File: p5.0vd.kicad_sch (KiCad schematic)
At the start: 11 parts, among them U14 LT3045xDD

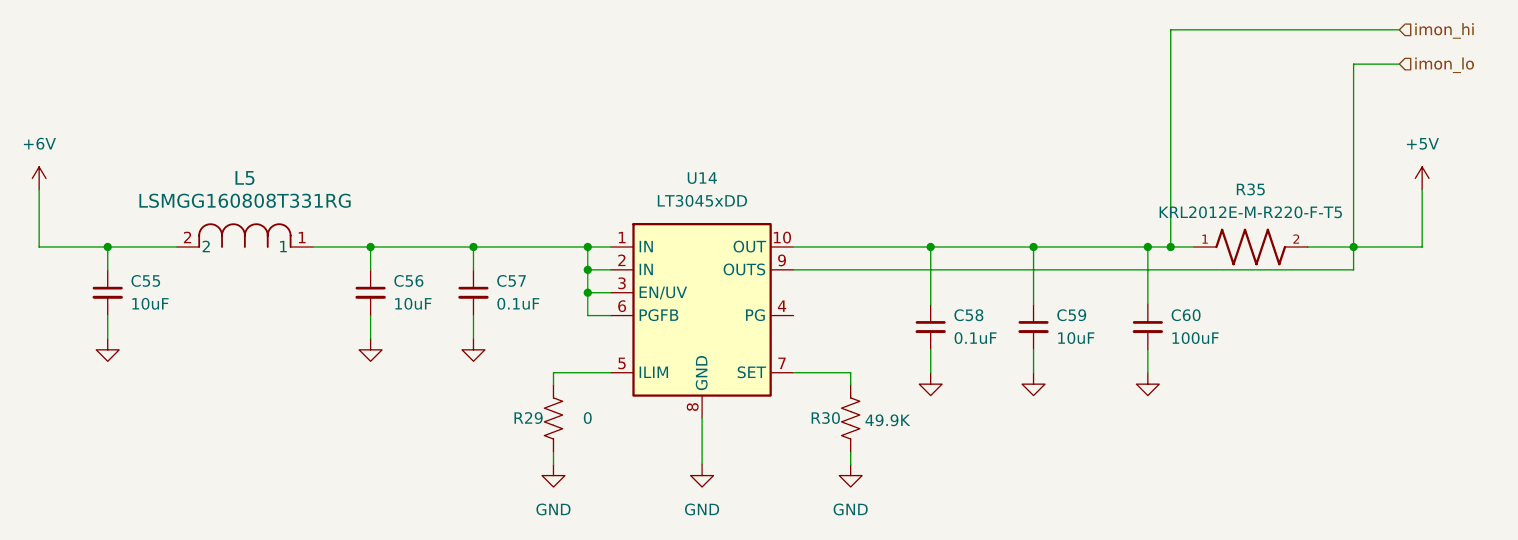
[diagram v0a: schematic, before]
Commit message: Add all 4 channels
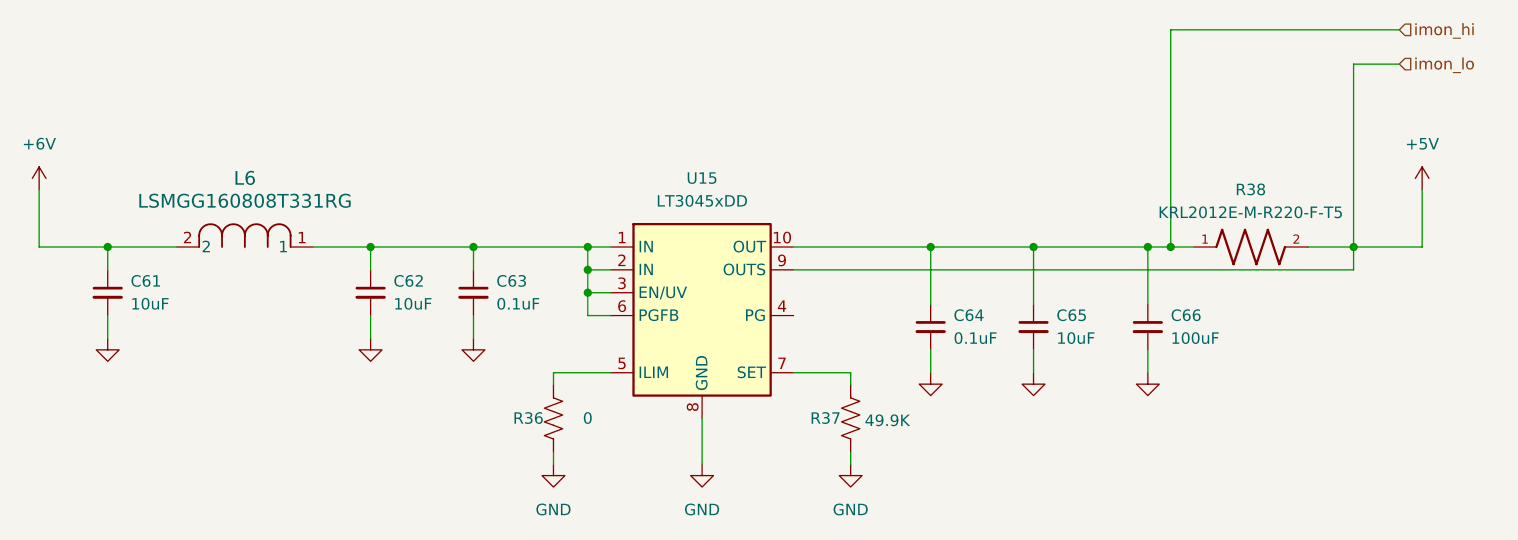
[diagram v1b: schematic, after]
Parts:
- renumbered C55 to C61, C56 to C62, C57 to C63, C58 to C64, C59 to C65, C60 to C66, L5 to L6, R29 to R36, R30 to R37, R35 to R38, U14 to U15
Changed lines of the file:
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@@
 		(dnp no)
 		(fields_autoplaced yes)
-		(property "Reference" "U14"
+		(property "Reference" "U15"
 			(at 144.78 63.5 0)
 			(effects
@@
 			(project "psc_carrier_brd"
 				(path "/40891cc8-bf64-41f4-8f69-a607d7b280eb/d1842e08-6ad7-4891-bdb3-3a3a498e2a30/71c60af7-80bf-4dda-a256-33ed6124b6e1"
-					(reference "U14")
+					(reference "U15")
 					(unit 1)
 				)
@@
 		(dnp no)
 		(fields_autoplaced yes)
-		(property "Reference" "#PWR0131"
+		(property "Reference" "#PWR0147"
 			(at 194.31 91.44 0)
 			(effects
@@
 			(project "psc_carrier_brd"
 				(path "/40891cc8-bf64-41f4-8f69-a607d7b280eb/d1842e08-6ad7-4891-bdb3-3a3a498e2a30/71c60af7-80bf-4dda-a256-33ed6124b6e1"
-					(reference "#PWR0131")
+					(reference "#PWR0147")
 					(unit 1)
 				)
@@
 		(dnp no)
 		(fields_autoplaced yes)
-		(property "Reference" "#PWR0129"
+		(property "Reference" "#PWR0145"
 			(at 170.18 91.44 0)
 			(effects
@@
 			(project "psc_carrier_brd"
 				(path "/40891cc8-bf64-41f4-8f69-a607d7b280eb/d1842e08-6ad7-4891-bdb3-3a3a498e2a30/71c60af7-80bf-4dda-a256-33ed6124b6e1"
-					(reference "#PWR0129")
+					(reference "#PWR0145")
 					(unit 1)
 				)
@@
 		(dnp no)
 		(fields_autoplaced yes)
-		(property "Reference" "#PWR0128"
+		(property "Reference" "#PWR0144"
 			(at 161.29 101.6 0)
 			(effects
@@
 			(project "psc_carrier_brd"
 				(path "/40891cc8-bf64-41f4-8f69-a607d7b280eb/d1842e08-6ad7-4891-bdb3-3a3a498e2a30/71c60af7-80bf-4dda-a256-33ed6124b6e1"
-					(reference "#PWR0128")
+					(reference "#PWR0144")
 					(unit 1)
 				)
@@
 		(on_board yes)
 		(dnp no)
-		(property "Reference" "R29"
+		(property "Reference" "R36"
 			(at 125.476 90.17 0)
 			(effects
@@
 			(project "psc_carrier_brd"
 				(path "/40891cc8-bf64-41f4-8f69-a607d7b280eb/d1842e08-6ad7-4891-bdb3-3a3a498e2a30/71c60af7-80bf-4dda-a256-33ed6124b6e1"
-					(reference "R29")
+					(reference "R36")
 					(unit 1)
 				)
@@
 		(on_board yes)
 		(dnp no)
-		(property "Reference" "C58"
+		(property "Reference" "C64"
 			(at 172.72 78.7462 0)
 			(effects
@@
 			(project "psc_carrier_brd"
 				(path "/40891cc8-bf64-41f4-8f69-a607d7b280eb/d1842e08-6ad7-4891-bdb3-3a3a498e2a30/71c60af7-80bf-4dda-a256-33ed6124b6e1"
-					(reference "C58")
+					(reference "C64")
 					(unit 1)
 				)
@@
 		(on_board yes)
 		(dnp no)
-		(property "Reference" "C55"
+		(property "Reference" "C61"
 			(at 81.28 74.9362 0)
 			(effects
@@
 			(project "psc_carrier_brd"
 				(path "/40891cc8-bf64-41f4-8f69-a607d7b280eb/d1842e08-6ad7-4891-bdb3-3a3a498e2a30/71c60af7-80bf-4dda-a256-33ed6124b6e1"
-					(reference "C55")
+					(reference "C61")
 					(unit 1)
 				)
@@
 		(on_board yes)
 		(dnp no)
-		(property "Reference" "C59"
+		(property "Reference" "C65"
 			(at 184.15 78.7462 0)
 			(effects
@@
 			(project "psc_carrier_brd"
 				(path "/40891cc8-bf64-41f4-8f69-a607d7b280eb/d1842e08-6ad7-4891-bdb3-3a3a498e2a30/71c60af7-80bf-4dda-a256-33ed6124b6e1"
-					(reference "C59")
+					(reference "C65")
 					(unit 1)
 				)
@@
 		(on_board yes)
 		(dnp no)
-		(property "Reference" "C56"
+		(property "Reference" "C62"
 			(at 110.49 74.9362 0)
 			(effects
@@
 			(project "psc_carrier_brd"
 				(path "/40891cc8-bf64-41f4-8f69-a607d7b280eb/d1842e08-6ad7-4891-bdb3-3a3a498e2a30/71c60af7-80bf-4dda-a256-33ed6124b6e1"
-					(reference "C56")
+					(reference "C62")
 					(unit 1)
 				)
@@
 		(dnp no)
 		(fields_autoplaced yes)
-		(property "Reference" "#PWR0126"
+		(property "Reference" "#PWR0142"
 			(at 128.27 101.6 0)
 			(effects
@@
 			(project "psc_carrier_brd"
 				(path "/40891cc8-bf64-41f4-8f69-a607d7b280eb/d1842e08-6ad7-4891-bdb3-3a3a498e2a30/71c60af7-80bf-4dda-a256-33ed6124b6e1"
-					(reference "#PWR0126")
+					(reference "#PWR0142")
 					(unit 1)
 				)
@@
 		(dnp no)
 		(fields_autoplaced yes)
-		(property "Reference" "#PWR0130"
+		(property "Reference" "#PWR0146"
 			(at 181.61 91.44 0)
 			(effects
@@
 			(project "psc_carrier_brd"
 				(path "/40891cc8-bf64-41f4-8f69-a607d7b280eb/d1842e08-6ad7-4891-bdb3-3a3a498e2a30/71c60af7-80bf-4dda-a256-33ed6124b6e1"
-					(reference "#PWR0130")
+					(reference "#PWR0146")
 					(unit 1)
 				)
@@
 		(dnp no)
 		(fields_autoplaced yes)
-		(property "Reference" "L5"
+		(property "Reference" "L6"
 			(at 93.98 63.5 0)
 			(effects
@@
 			(project "psc_carrier_brd"
 				(path "/40891cc8-bf64-41f4-8f69-a607d7b280eb/d1842e08-6ad7-4891-bdb3-3a3a498e2a30/71c60af7-80bf-4dda-a256-33ed6124b6e1"
-					(reference "L5")
+					(reference "L6")
 					(unit 1)
 				)
@@
 		(dnp no)
 		(fields_autoplaced yes)
-		(property "Reference" "#PWR0125"
+		(property "Reference" "#PWR0141"
 			(at 119.38 87.63 0)
 			(effects
@@
 			(project "psc_carrier_brd"
 				(path "/40891cc8-bf64-41f4-8f69-a607d7b280eb/d1842e08-6ad7-4891-bdb3-3a3a498e2a30/71c60af7-80bf-4dda-a256-33ed6124b6e1"
-					(reference "#PWR0125")
+					(reference "#PWR0141")
 					(unit 1)
 				)
@@
 		(on_board yes)
 		(dnp no)
-		(property "Reference" "R30"
+		(property "Reference" "R37"
 			(at 158.496 90.17 0)
 			(effects
@@
 			(project "psc_carrier_brd"
 				(path "/40891cc8-bf64-41f4-8f69-a607d7b280eb/d1842e08-6ad7-4891-bdb3-3a3a498e2a30/71c60af7-80bf-4dda-a256-33ed6124b6e1"
-					(reference "R30")
+					(reference "R37")
 					(unit 1)
 				)
@@
 		(dnp no)
 		(fields_autoplaced yes)
-		(property "Reference" "#PWR0124"
+		(property "Reference" "#PWR0140"
 			(at 107.95 87.63 0)
 			(effects
@@
 			(project "psc_carrier_brd"
 				(path "/40891cc8-bf64-41f4-8f69-a607d7b280eb/d1842e08-6ad7-4891-bdb3-3a3a498e2a30/71c60af7-80bf-4dda-a256-33ed6124b6e1"
-					(reference "#PWR0124")
+					(reference "#PWR0140")
 					(unit 1)
 				)
@@
 		(dnp no)
 		(fields_autoplaced yes)
-		(property "Reference" "#PWR0127"
+		(property "Reference" "#PWR0143"
 			(at 144.78 101.6 0)
 			(effects
@@
 			(project "psc_carrier_brd"
 				(path "/40891cc8-bf64-41f4-8f69-a607d7b280eb/d1842e08-6ad7-4891-bdb3-3a3a498e2a30/71c60af7-80bf-4dda-a256-33ed6124b6e1"
-					(reference "#PWR0127")
+					(reference "#PWR0143")
 					(unit 1)
 				)
@@
 		(dnp no)
 		(fields_autoplaced yes)
-		(property "Reference" "#PWR0132"
+		(property "Reference" "#PWR0148"
 			(at 224.79 68.58 0)
 			(effects
@@
 			(project ""
 				(path "/40891cc8-bf64-41f4-8f69-a607d7b280eb/d1842e08-6ad7-4891-bdb3-3a3a498e2a30/71c60af7-80bf-4dda-a256-33ed6124b6e1"
-					(reference "#PWR0132")
+					(reference "#PWR0148")
 					(unit 1)
 				)
@@
 		(on_board yes)
 		(dnp no)
-		(property "Reference" "C60"
+		(property "Reference" "C66"
 			(at 196.85 78.7462 0)
 			(effects
@@
 			(project "psc_carrier_brd"
 				(path "/40891cc8-bf64-41f4-8f69-a607d7b280eb/d1842e08-6ad7-4891-bdb3-3a3a498e2a30/71c60af7-80bf-4dda-a256-33ed6124b6e1"
-					(reference "C60")
+					(reference "C66")
 					(unit 1)
 				)
@@
 		(on_board yes)
 		(dnp no)
-		(property "Reference" "C57"
+		(property "Reference" "C63"
 			(at 121.92 74.9362 0)
 			(effects
@@
 			(project "psc_carrier_brd"
 				(path "/40891cc8-bf64-41f4-8f69-a607d7b280eb/d1842e08-6ad7-4891-bdb3-3a3a498e2a30/71c60af7-80bf-4dda-a256-33ed6124b6e1"
-					(reference "C57")
+					(reference "C63")
 					(unit 1)
 				)
@@
 		(dnp no)
 		(fields_autoplaced yes)
-		(property "Reference" "#PWR0122"
+		(property "Reference" "#PWR0138"
 			(at 71.12 68.58 0)
 			(effects
@@
 			(project "psc_carrier_brd"
 				(path "/40891cc8-bf64-41f4-8f69-a607d7b280eb/d1842e08-6ad7-4891-bdb3-3a3a498e2a30/71c60af7-80bf-4dda-a256-33ed6124b6e1"
-					(reference "#PWR0122")
+					(reference "#PWR0138")
 					(unit 1)
 				)
@@
 		(dnp no)
 		(fields_autoplaced yes)
-		(property "Reference" "#PWR0123"
+		(property "Reference" "#PWR0139"
 			(at 78.74 87.63 0)
 			(effects
@@
 			(project "psc_carrier_brd"
 				(path "/40891cc8-bf64-41f4-8f69-a607d7b280eb/d1842e08-6ad7-4891-bdb3-3a3a498e2a30/71c60af7-80bf-4dda-a256-33ed6124b6e1"
-					(reference "#PWR0123")
+					(reference "#PWR0139")
 					(unit 1)
 				)
@@
 		(dnp no)
 		(fields_autoplaced yes)
-		(property "Reference" "R35"
+		(property "Reference" "R38"
 			(at 205.74 64.77 0)
 			(effects
@@
 			(project "psc_carrier_brd"
 				(path "/40891cc8-bf64-41f4-8f69-a607d7b280eb/d1842e08-6ad7-4891-bdb3-3a3a498e2a30/71c60af7-80bf-4dda-a256-33ed6124b6e1"
-					(reference "R35")
-					(unit 1)
-				)
+					(reference "R38")
+					(unit 1)
+				)
